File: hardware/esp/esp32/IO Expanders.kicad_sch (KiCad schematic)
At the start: 4 parts, among them U1 MCP23008-E/ML, U4 MCP23008-E/ML

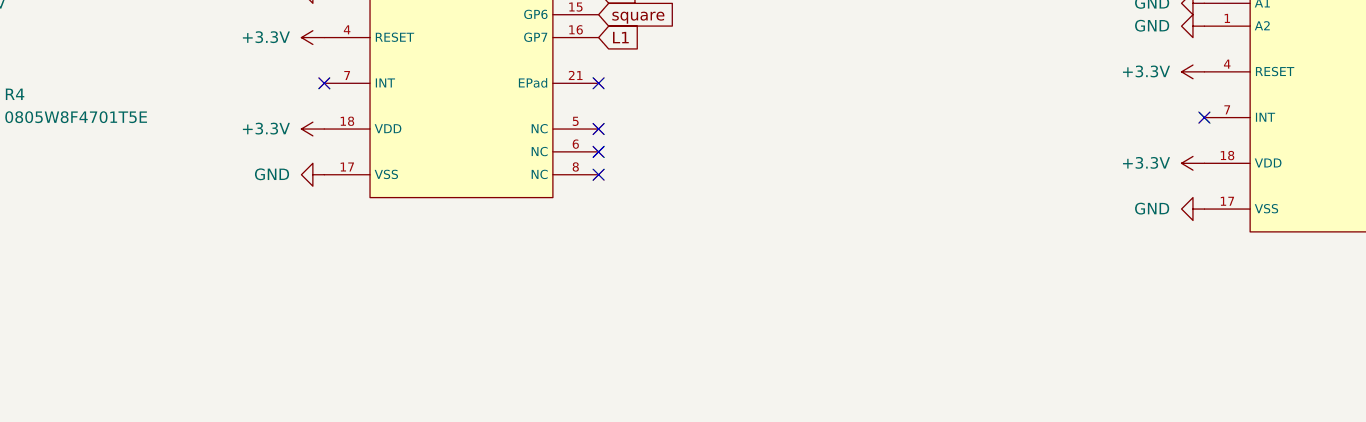
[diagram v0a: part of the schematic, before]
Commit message: Added hardware 0.2 - Added right FPC
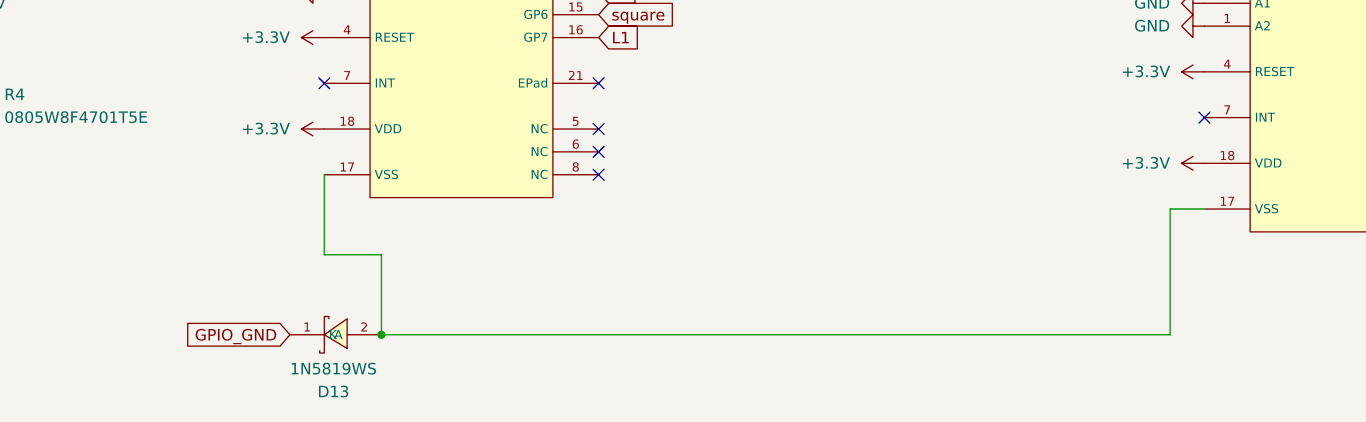
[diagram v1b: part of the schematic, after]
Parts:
- added D13: 1N5819WS, JLCPCB_footprint:SOD-323_L1.8-W1.3-LS2.5-RD, symbol JLCPCB_schematic:1N5819WS
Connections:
- net GND: no longer U1.17 (VSS), U4.17 (VSS)
- new net: D13.2 (A), U1.17 (VSS), U4.17 (VSS)
- new net GPIO_GND: D13.1 (K)
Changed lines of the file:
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@@
+	)
+	(junction
+		(at 111.76 128.27)
+		(diameter 0)
+		(color 0 0 0 0)
 	)
 	(junction
@@
 	(wire
 		(pts
+			(xy 199.39 114.3) (xy 199.39 128.27)
+		)
+		(stroke
+			(width 0)
+			(type default)
+		)
+	)
+	(wire
+		(pts
 			(xy 73.66 86.36) (xy 87.63 86.36)
 		)
@@
 	(wire
 		(pts
+			(xy 203.2 114.3) (xy 199.39 114.3)
+		)
+		(stroke
+			(width 0)
+			(type default)
+		)
+	)
+	(wire
+		(pts
 			(xy 63.5 92.71) (xy 63.5 88.9)
 		)
@@
 	(wire
 		(pts
+			(xy 199.39 128.27) (xy 111.76 128.27)
+		)
+		(stroke
+			(width 0)
+			(type default)
+		)
+	)
+	(wire
+		(pts
 			(xy 67.31 96.52) (xy 67.31 97.79)
 		)
@@
 	(wire
 		(pts
+			(xy 105.41 110.49) (xy 105.41 119.38)
+		)
+		(stroke
+			(width 0)
+			(type default)
+		)
+	)
+	(wire
+		(pts
 			(xy 105.41 80.01) (xy 90.17 80.01)
 		)
@@
 	(wire
 		(pts
+			(xy 105.41 119.38) (xy 111.76 119.38)
+		)
+		(stroke
+			(width 0)
+			(type default)
+		)
+	)
+	(wire
+		(pts
 			(xy 53.34 92.71) (xy 63.5 92.71)
 		)
@@
 		(pts
 			(xy 73.66 85.09) (xy 73.66 86.36)
+		)
+		(stroke
+			(width 0)
+			(type default)
+		)
+	)
+	(wire
+		(pts
+			(xy 111.76 119.38) (xy 111.76 128.27)
 		)
 		(stroke
@@
 				)
 				(justify left)
+				(hide yes)
+			)
+		)
+	)
+	(global_label "GPIO_GND"
+		(shape input)
+		(at 101.6 128.27 180)
+		(fields_autoplaced yes)
+		(effects
+			(font
+				(size 1.27 1.27)
+			)
+			(justify right)
+		)
+		(property "Intersheetrefs" "${INTERSHEET_REFS}"
+			(at 89.3014 128.27 0)
+			(effects
+				(font
+					(size 1.27 1.27)
+				)
+				(justify right)
 				(hide yes)
 			)
@@
 	)
 	(symbol
-		(lib_id "power:GND")
-		(at 203.2 114.3 270)
-		(unit 1)
-		(exclude_from_sim no)
-		(in_bom yes)
-		(on_board yes)
-		(dnp no)
-		(fields_autoplaced yes)
-		(property "Reference" "#PWR050"
-			(at 196.85 114.3 0)
-			(effects
-				(font
-					(size 1.27 1.27)
-				)
-				(hide yes)
-			)
-		)
-		(property "Value" "GND"
-			(at 199.39 114.2999 90)
-			(effects
-				(font
-					(size 1.27 1.27)
-				)
-				(justify right)
-			)
-		)
-		(property "Footprint" ""
-			(at 203.2 114.3 0)
-			(effects
-				(font
-					(size 1.27 1.27)
-				)
-				(hide yes)
-			)
-		)
-		(property "Datasheet" ""
-			(at 203.2 114.3 0)
-			(effects
-				(font
-					(size 1.27 1.27)
-				)
-				(hide yes)
-			)
-		)
-		(property "Description" "Power symbol creates a global label with name \"GND\" , ground"
-			(at 203.2 114.3 0)
-			(effects
-				(font
-					(size 1.27 1.27)
-				)
-				(hide yes)
-			)
-		)
-		(pin "1"
-		)
-		(instances
-			(project "esp32"
-				(path "/3a9f3299-35f4-4d62-9438-2986d1fa401f/69246014-e69c-483a-8e99-10eb89618c95"
-					(reference "#PWR050")
-					(unit 1)
-				)
-			)
-		)
-	)
-	(symbol
 		(lib_id "JLCPCB_schematic:0805W8F4701T5E")
 		(at 73.66 80.01 90)
@@
 	)
 	(symbol
+		(lib_id "JLCPCB_schematic:1N5819WS")
+		(at 106.68 128.27 0)
+		(mirror x)
+		(unit 1)
+		(exclude_from_sim no)
+		(in_bom yes)
+		(on_board yes)
+		(dnp no)
+		(fields_autoplaced yes)
+		(property "Reference" "D13"
+			(at 106.426 134.62 0)
+			(effects
+				(font
+					(size 1.27 1.27)
+				)
+			)
+		)
+		(property "Value" "1N5819WS"
+			(at 106.426 132.08 0)
+			(effects
+				(font
+					(size 1.27 1.27)
+				)
+			)
+		)
+		(property "Footprint" "JLCPCB_footprint:SOD-323_L1.8-W1.3-LS2.5-RD"
+			(at 106.68 118.11 0)
+			(effects
+				(font
+					(size 1.27 1.27)
+					(italic yes)
+				)
+				(hide yes)
+			)
+		)
+		(property "Datasheet" "https://item.szlcsc.com/295156.html"
+			(at 104.394 128.397 0)
+			(effects
+				(font
+					(size 1.27 1.27)
+				)
+				(justify left)
+				(hide yes)
+			)
+		)
+		(property "Description" "shotkey diode"
+			(at 106.68 128.27 0)
+			(effects
+				(font
+					(size 1.27 1.27)
+				)
+				(hide yes)
+			)
+		)
+		(property "LCSC" "C191023"
+			(at 106.68 128.27 0)
+			(effects
+				(font
+					(size 1.27 1.27)
+				)
+				(hide yes)
+			)
+		)
+		(pin "1"
+		)
+		(pin "2"
+		)
+		(instances
+			(project "esp32"
+				(path "/3a9f3299-35f4-4d62-9438-2986d1fa401f/69246014-e69c-483a-8e99-10eb89618c95"
+					(reference "D13")
+					(unit 1)
+				)
+			)
+		)
+	)
+	(symbol
 		(lib_id "power:+3.3V")
 		(at 105.41 95.25 90)
@@
 					(unit 1)
 				)
-			)
-		)
-	)
-	(symbol
-		(lib_id "power:GND")
-		(at 105.41 110.49 270)
-		(unit 1)
-		(exclude_from_sim no)
-		(in_bom yes)
-		(on_board yes)
-		(dnp no)
-		(fields_autoplaced yes)
-		(property "Reference" "#PWR042"
-			(at 99.06 110.49 0)
-			(effects
-				(font
-					(size 1.27 1.27)
-				)
-				(hide yes)
-			)
-		)
-		(property "Value" "GND"
-			(at 101.6 110.4899 90)
-			(effects
-				(font
-					(size 1.27 1.27)
-				)
-				(justify right)
-			)
-		)
-		(property "Footprint" ""
-			(at 105.41 110.49 0)
-			(effects
-				(font
-					(size 1.27 1.27)
-				)
-				(hide yes)
-			)
-		)
-		(property "Datasheet" ""
-			(at 105.41 110.49 0)
-			(effects
-				(font
-					(size 1.27 1.27)
-				)
-				(hide yes)
-			)
-		)
-		(property "Description" "Power symbol creates a global label with name \"GND\" , ground"
-			(at 105.41 110.49 0)
-			(effects
-				(font
-					(size 1.27 1.27)
-				)
-				(hide yes)
-			)
-		)
-		(pin "1"
-		)
-		(instances
-			(project "esp32"
-				(path "/3a9f3299-35f4-4d62-9438-2986d1fa401f/69246014-e69c-483a-8e99-10eb89618c95"
-					(reference "#PWR042")
-					(unit 1)
-				)

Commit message: stuff
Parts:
- removed D13: 1N5819WS, JLCPCB_footprint:SOD-323_L1.8-W1.3-LS2.5-RD, symbol JLCPCB_schematic:1N5819WS
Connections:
- net GND: now also U1.17 (VSS), U4.17 (VSS)
